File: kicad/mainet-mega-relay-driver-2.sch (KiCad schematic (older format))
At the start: 8 parts, among them J31 Screw_Terminal_01x03, K2 SANYOU_SRD_Form_C, Q2 2N3904, U3 4N37

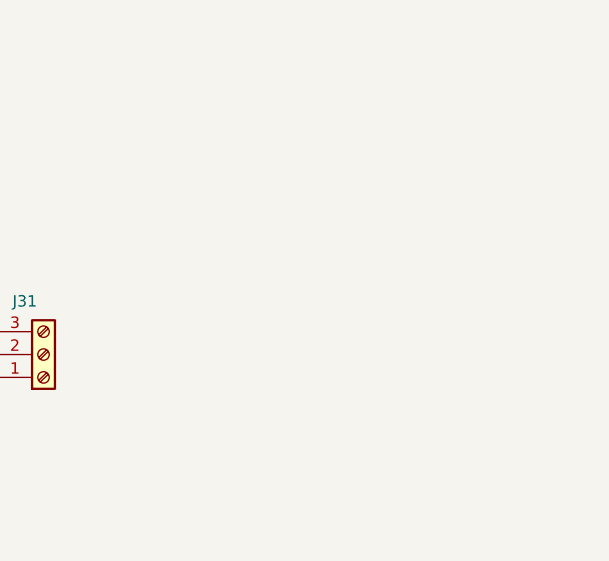
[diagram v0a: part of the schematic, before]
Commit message: KICAD: Actualizar esquemáticos
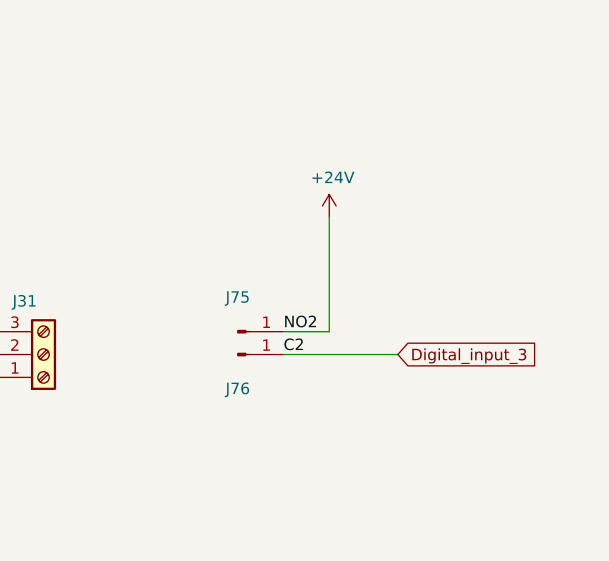
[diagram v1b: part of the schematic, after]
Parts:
- added J75, J76: Conn_01x01_Male, symbol Connector:Conn_01x01_Male
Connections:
- net C2 renamed Digital_input_3
- net Digital_input_3: now also J76.1 (Pin_1)
- net NO2 renamed +24V
- net +24V: now also J75.1 (Pin_1)
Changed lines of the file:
@@
 encoding utf-8
 Sheet 8 21
-Title "Mainet-mega -- "
-Date "2021-04-06"
+Title "Mainet-mega -- runForwardControl"
+Date "2021-04-07"
 Rev "1.0"
 Comp "Tovenca"
@@
 Text Notes 3200 2300 0    50   ~ 0
 VCC:\nSalida +5V del Arduino
+$Comp
+L Connector:Conn_01x01_Male J75
+U 1 1 606EB603
+P 8950 3650
+F 0 "J75" H 8950 3800 50  0000 C CNN
+F 1 "Conn_01x01_Male" H 9058 3740 50  0001 C CNN
+F 2 "" H 8950 3650 50  0001 C CNN
+F 3 "~" H 8950 3650 50  0001 C CNN
+	1    8950 3650
+	1    0    0    -1
+$EndComp
+$Comp
+L Connector:Conn_01x01_Male J76
+U 1 1 606EBE14
+P 8950 3750
+F 0 "J76" H 8950 3600 50  0000 C CNN
+F 1 "Conn_01x01_Male" H 9058 3840 50  0001 C CNN
+F 2 "" H 8950 3750 50  0001 C CNN
+F 3 "~" H 8950 3750 50  0001 C CNN
+	1    8950 3750
+	1    0    0    -1
+$EndComp
+$Comp
+L power:+24V #PWR0101
+U 1 1 606EC3A6
+P 9350 3150
+F 0 "#PWR0101" H 9350 3000 50  0001 C CNN
+F 1 "+24V" H 9365 3323 50  0000 C CNN
+F 2 "" H 9350 3150 50  0001 C CNN
+F 3 "" H 9350 3150 50  0001 C CNN
+	1    9350 3150
+	1    0    0    -1
+$EndComp
+Wire Wire Line
+	9350 3150 9350 3650
+Wire Wire Line
+	9350 3650 9150 3650
+Text Label 9150 3650 0    50   ~ 0
+NO2
+Text Label 9150 3750 0    50   ~ 0
+C2
+Wire Wire Line
+	9150 3750 9650 3750
+Text GLabel 9650 3750 2    50   Input ~ 0
+Digital_input_3
 $EndSCHEMATC

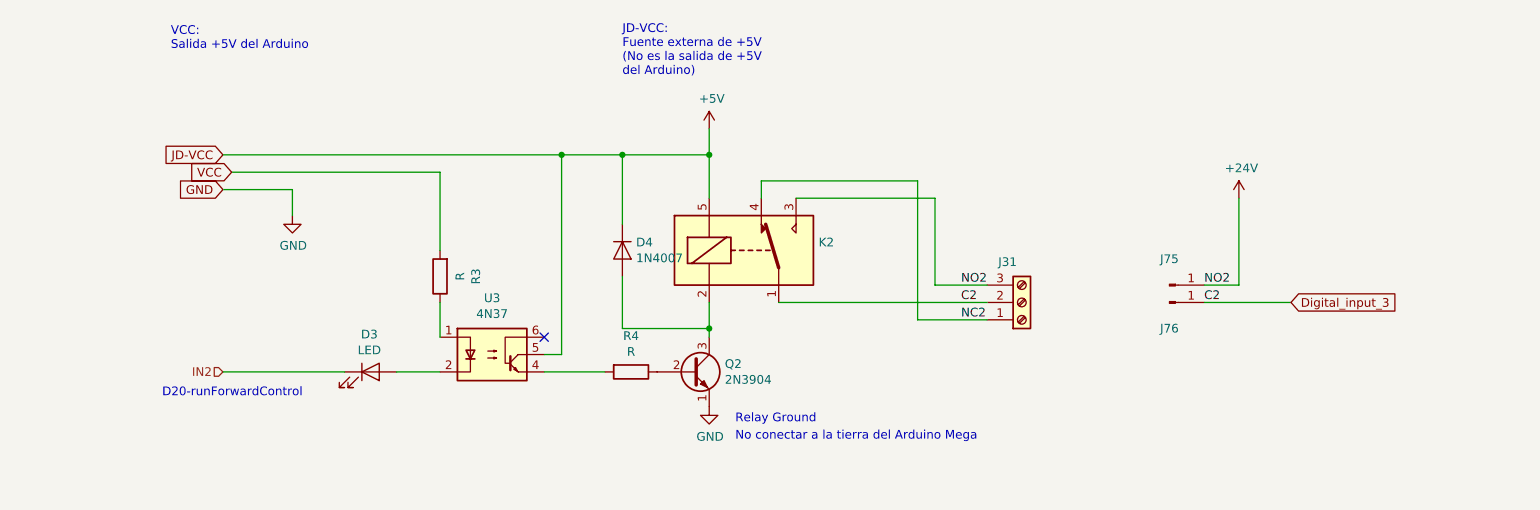
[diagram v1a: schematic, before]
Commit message: KICAD: Modificar esquemático
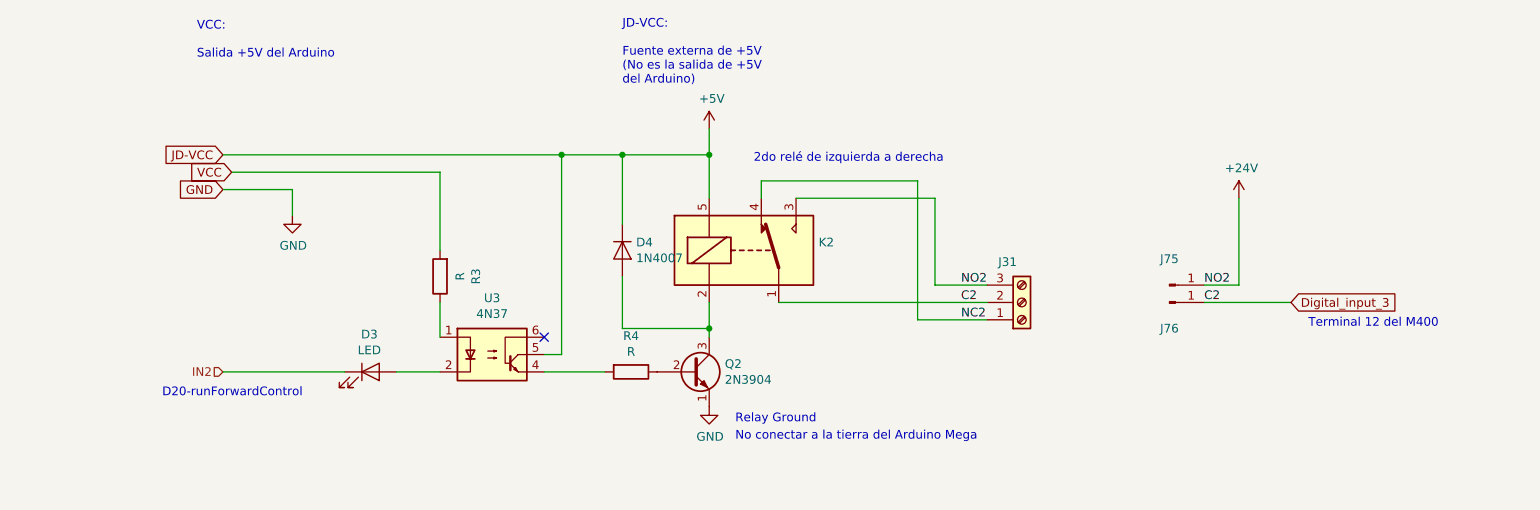
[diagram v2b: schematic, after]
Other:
- note added: "2do relé de izquierda a derecha"
- note added: "JD-VCC:\n\nFuente externa de +5V\n(No es la salida de +5V \ndel Arduino)"
- note added: "Terminal 12 del M400"
- note added: "VCC:\n\nSalida +5V del Arduino"
- note removed: "JD-VCC:\nFuente externa de +5V\n(No es la salida de +5V \ndel Arduino)"
- note removed: "VCC:\nSalida +5V del Arduino"
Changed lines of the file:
@@
 EESchema Schematic File Version 4
+LIBS:mainet-mega-cache
 EELAYER 30 0
 EELAYER END
@@
 Sheet 8 21
 Title "Mainet-mega -- runForwardControl"
-Date "2021-04-07"
+Date "2021-06-16"
 Rev "1.0"
 Comp "Tovenca"
@@
 Text Notes 3150 4300 0    50   ~ 0
 D20-runForwardControl
-Text Notes 5800 2450 0    50   ~ 0
-JD-VCC:\nFuente externa de +5V\n(No es la salida de +5V \ndel Arduino)
-Text Notes 3200 2300 0    50   ~ 0
-VCC:\nSalida +5V del Arduino
+Text Notes 5800 2500 0    50   ~ 0
+JD-VCC:\n\nFuente externa de +5V\n(No es la salida de +5V \ndel Arduino)
+Text Notes 3350 2350 0    50   ~ 0
+VCC:\n\nSalida +5V del Arduino
 $Comp
 L Connector:Conn_01x01_Male J75
@@
 Text GLabel 9650 3750 2    50   Input ~ 0
 Digital_input_3
+Text Notes 7650 2950 2    50   ~ 0
+2do relé de izquierda a derecha
+Text Notes 10500 3900 2    50   ~ 0
+Terminal 12 del M400
 $EndSCHEMATC

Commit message: KICAD: Actualizar archivos del módulo de relés
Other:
- note added: "Relay Ground\nNo conectar a la tierra\ndel Arduino Mega\n"
- note removed: "No conectar a la tierra del Arduino Mega\n"
- note removed: "Relay Ground\n"
- moved on the sheet: D3, D4, J31, J75, J76, K2, Q2, R3, R4, U3

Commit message: KICAD: Agregar cambios esquemáticos
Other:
- note added: "Nota:\nEsta tensión de 24V la proporciona el M400, \nen los terminales 9 y 17."
- note added: "Terminal 9 del M400"
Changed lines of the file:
@@
 Sheet 8 22
 Title "Mainet-mega -- runForwardControl"
-Date "2021-06-17"
+Date "2021-06-18"
 Rev "1.0"
 Comp "Tovenca"
@@
 $EndComp
 Wire Wire Line
-	8600 3150 8600 3650
+	8600 3150 8600 3250
 Wire Wire Line
 	8600 3650 8400 3650
@@
 Text Notes 5200 4850 0    50   ~ 0
 Relay Ground\nNo conectar a la tierra\ndel Arduino Mega\n
+Text GLabel 8900 3250 2    50   Input ~ 0
+24V_user
+Wire Wire Line
+	8600 3250 8900 3250
+Connection ~ 8600 3250
+Wire Wire Line
+	8600 3250 8600 3650
+Text Notes 8900 3400 0    50   ~ 0
+Terminal 9 del M400
+Text Notes 8900 3650 0    50   ~ 0
+Nota:\nEsta tensión de 24V la proporciona el M400, \nen los terminales 9 y 17.
 $EndSCHEMATC
